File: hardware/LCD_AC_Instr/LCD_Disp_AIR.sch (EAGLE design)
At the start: 38 parts, among them IC3 TC10553.3V, J1 12V input, Q1 16MHz, SW1 ENCODER_SW1-PEC12, U1 ATMEGA328P-AU(R), U3 78M05

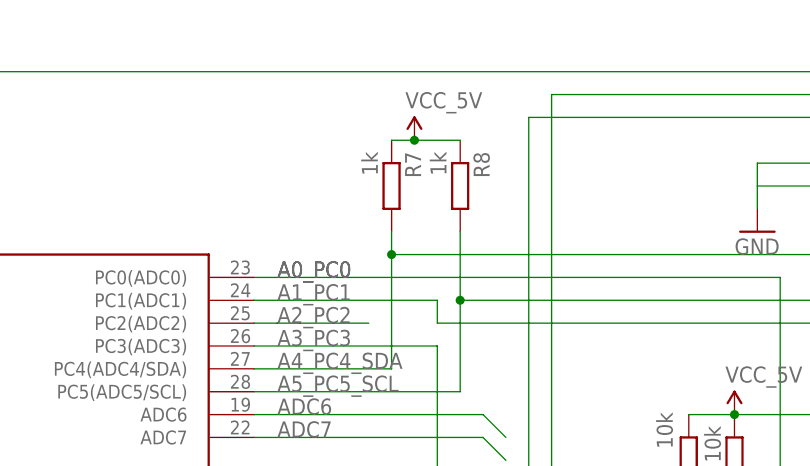
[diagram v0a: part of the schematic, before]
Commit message: changed resistor value in i2C lines to 100K to allow for the old style BMP085 which is not 5V compatible
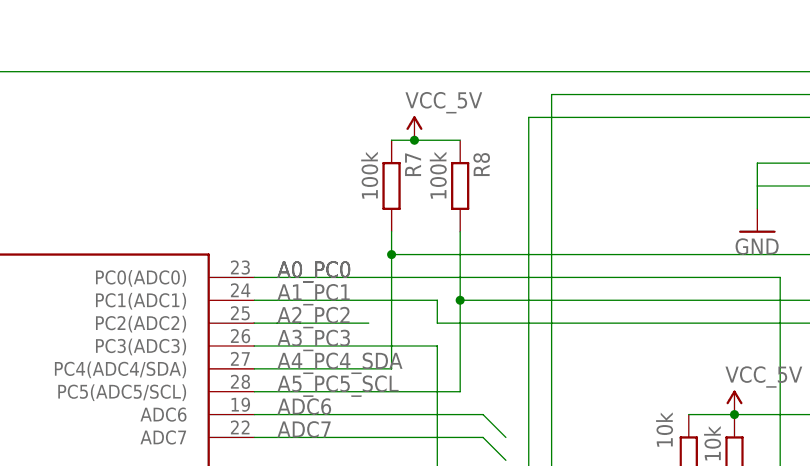
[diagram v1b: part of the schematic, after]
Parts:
- R7, R8: value 1k -> 100k
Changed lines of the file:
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@@
 <part name="R5" library="dp_devices" deviceset="RESISTOR" device="-0603" value="10k"/>
 <part name="R6" library="dp_devices" deviceset="RESISTOR" device="-0603"/>
-<part name="R7" library="dp_devices" deviceset="RESISTOR" device="-0603" value="1k"/>
-<part name="R8" library="dp_devices" deviceset="RESISTOR" device="-0603" value="1k"/>
+<part name="R7" library="dp_devices" deviceset="RESISTOR" device="-0603" value="100k"/>
+<part name="R8" library="dp_devices" deviceset="RESISTOR" device="-0603" value="100k"/>
 <part name="R9" library="SparkFun" deviceset="RESISTOR" device="0603" value="10K"/>
 <part name="C3" library="SparkFun" deviceset="CAP" device="0805" value="0.1uF"/>

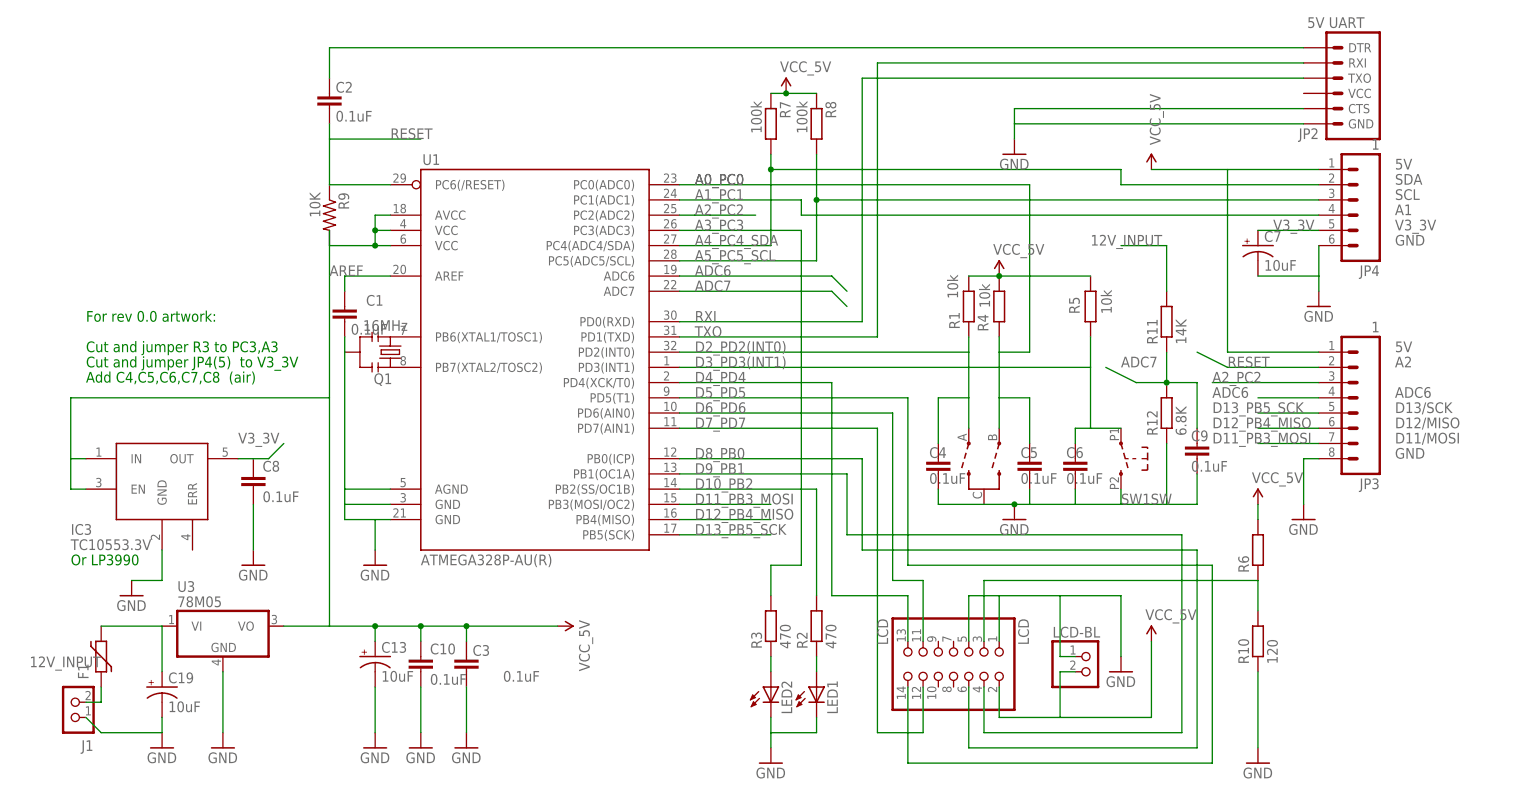
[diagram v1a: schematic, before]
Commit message: Added Geiger counter schematic and layout Added copy arduino sketch from rhelectronics
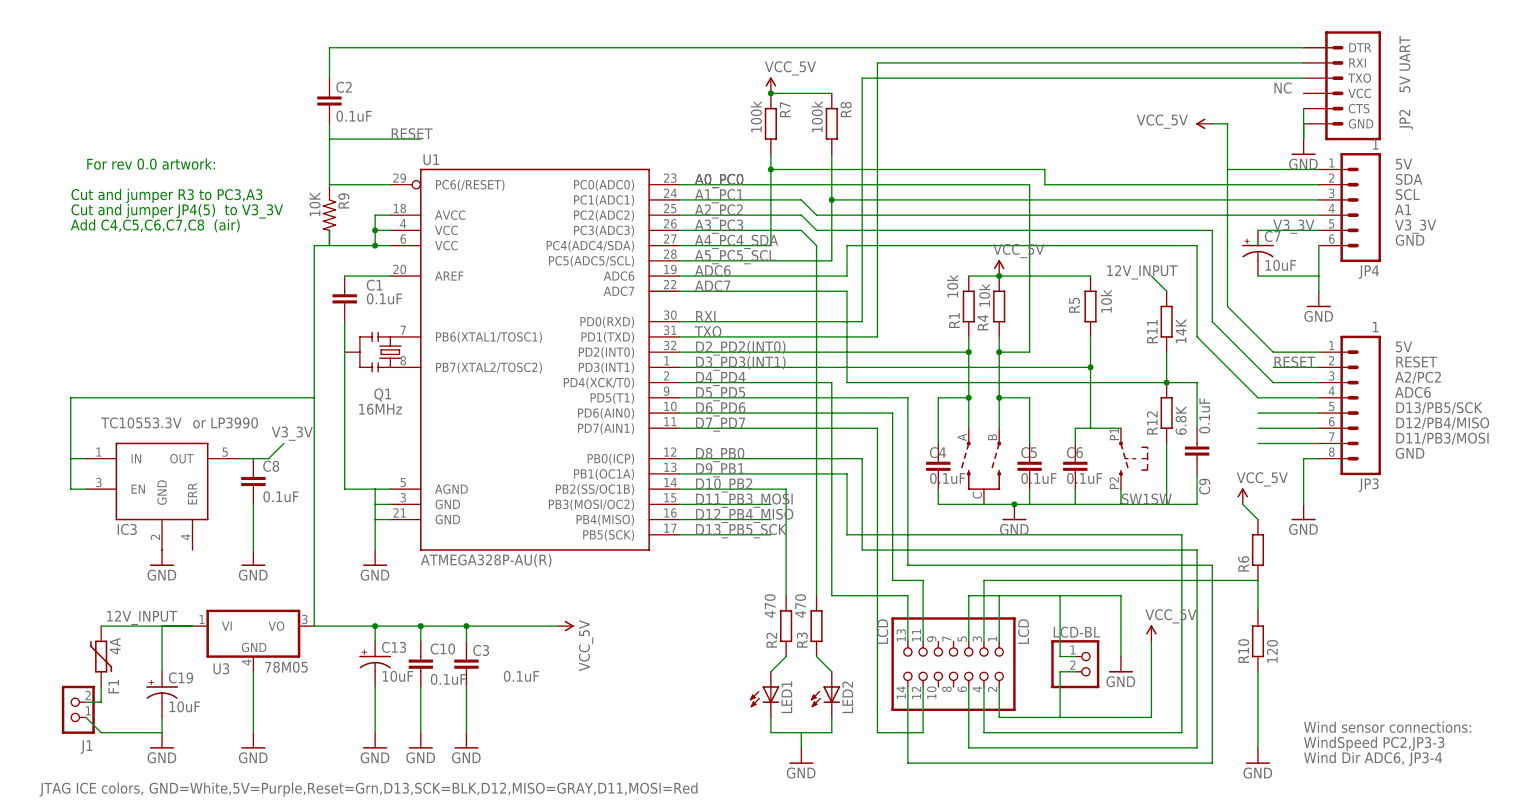
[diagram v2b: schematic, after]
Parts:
- F1: value (none) -> 4A
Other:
- note added: "A2/PC2"
- note added: "D11/PB3/MOSI"
- note added: "D12/PB4/MISO"
- note added: "D13/PB5/SCK"
- note added: "JTAG ICE colors, GND=White,5V=Purple,Reset=Grn,D13,SCK=BLK,D12,MISO=GRAY,D11,MOSI=Red"
- note added: "NC"
- note added: "Wind Dir ADC6, JP3-4"
- note added: "Wind sensor connections:"
- note added: "WindSpeed PC2,JP3-3"
- note added: "or LP3990"
- note removed: "A2"
- note removed: "D11/MOSI"
- note removed: "D12/MISO"
- note removed: "D13/SCK"
- note removed: "Or LP3990"
- moved on the sheet: C1, LED1, LED2, R2, R3, R8, U3
